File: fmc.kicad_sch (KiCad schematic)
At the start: 2 parts, among them P1 ASP-134604-01, P2 ASP-134604-01

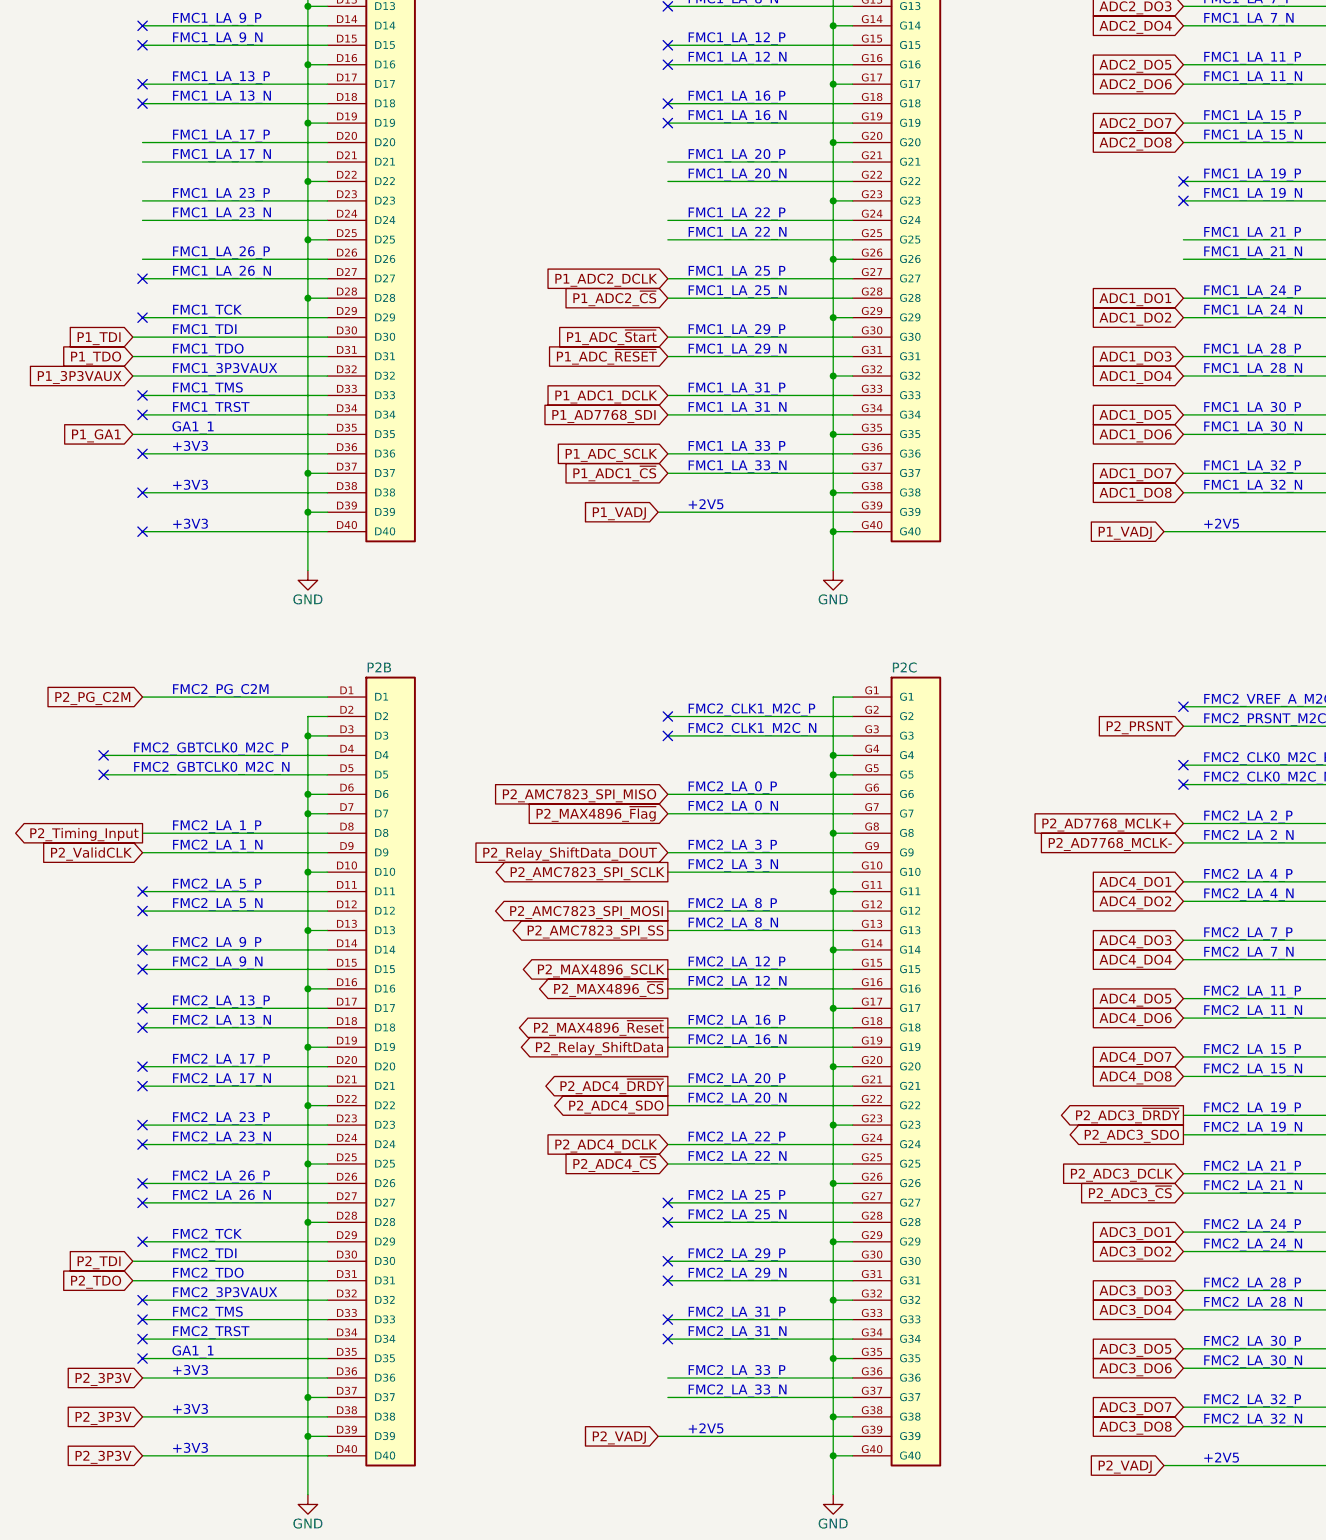
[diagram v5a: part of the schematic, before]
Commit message: Push Version before ADC change from 1.8V to 2.5V I/O
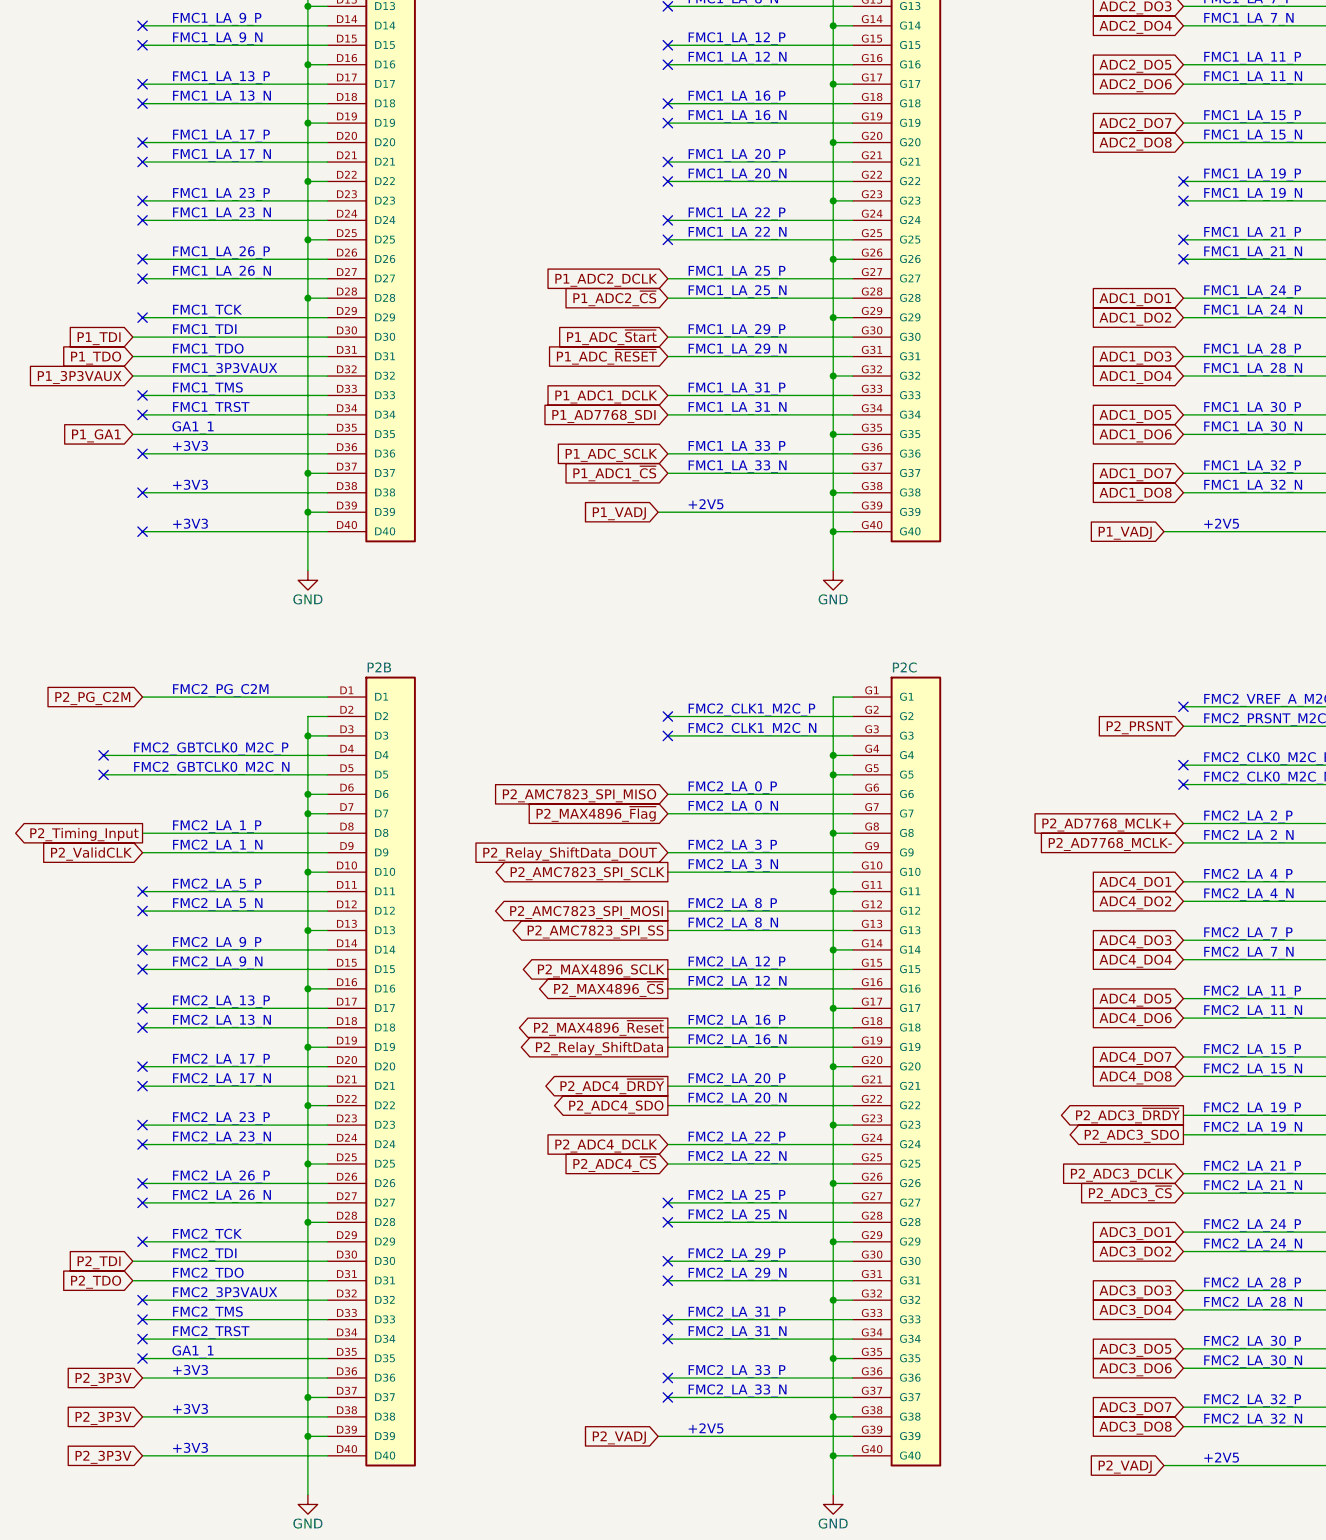
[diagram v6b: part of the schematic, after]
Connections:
- no-connect marks 95 -> 108
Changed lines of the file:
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@@
   )
   (no_connect (at 157.48 49.53))
+  (no_connect (at 293.37 82.55))
   (no_connect (at 157.48 102.87))
   (no_connect (at 87.63 57.15))
@@
   (no_connect (at 87.63 36.83))
   (no_connect (at 157.48 177.8))
+  (no_connect (at 226.06 82.55))
   (no_connect (at 293.37 143.51))
   (no_connect (at 87.63 204.47))
   (no_connect (at 293.37 151.13))
   (no_connect (at 226.06 41.91))
+  (no_connect (at 157.48 80.01))
   (no_connect (at 87.63 146.05))
   (no_connect (at 152.4 31.75))
@@
   (no_connect (at 157.48 185.42))
   (no_connect (at 157.48 213.36))
+  (no_connect (at 226.06 233.68))
   (no_connect (at 87.63 173.99))
   (no_connect (at 157.48 200.66))
   (no_connect (at 87.63 166.37))
+  (no_connect (at 157.48 69.85))
   (no_connect (at 87.63 207.01))
   (no_connect (at 87.63 176.53))
   (no_connect (at 157.48 193.04))
+  (no_connect (at 157.48 77.47))
   (no_connect (at 157.48 39.37))
   (no_connect (at 226.06 24.13))
@@
   (no_connect (at 226.06 218.44))
   (no_connect (at 226.06 44.45))
+  (no_connect (at 226.06 231.14))
+  (no_connect (at 226.06 74.93))
   (no_connect (at 226.06 67.31))
   (no_connect (at 293.37 74.93))
@@
   (no_connect (at 226.06 64.77))
   (no_connect (at 157.48 46.99))
+  (no_connect (at 157.48 72.39))
   (no_connect (at 293.37 21.59))
   (no_connect (at 87.63 163.83))
   (no_connect (at 157.48 115.57))
+  (no_connect (at 157.48 85.09))
   (no_connect (at 157.48 64.77))
   (no_connect (at 293.37 153.67))
@@
   (no_connect (at 152.4 29.21))
   (no_connect (at 157.48 62.23))
+  (no_connect (at 226.06 80.01))
   (no_connect (at 152.4 149.86))
   (no_connect (at 226.06 208.28))
@@
   (no_connect (at 226.06 223.52))
   (no_connect (at 87.63 46.99))
+  (no_connect (at 293.37 85.09))
   (no_connect (at 87.63 26.67))
   (no_connect (at 87.63 77.47))
@@
   (no_connect (at 157.48 198.12))
   (no_connect (at 157.48 223.52))
+  (no_connect (at 226.06 72.39))
   (no_connect (at 157.48 105.41))
   (no_connect (at 226.06 144.78))

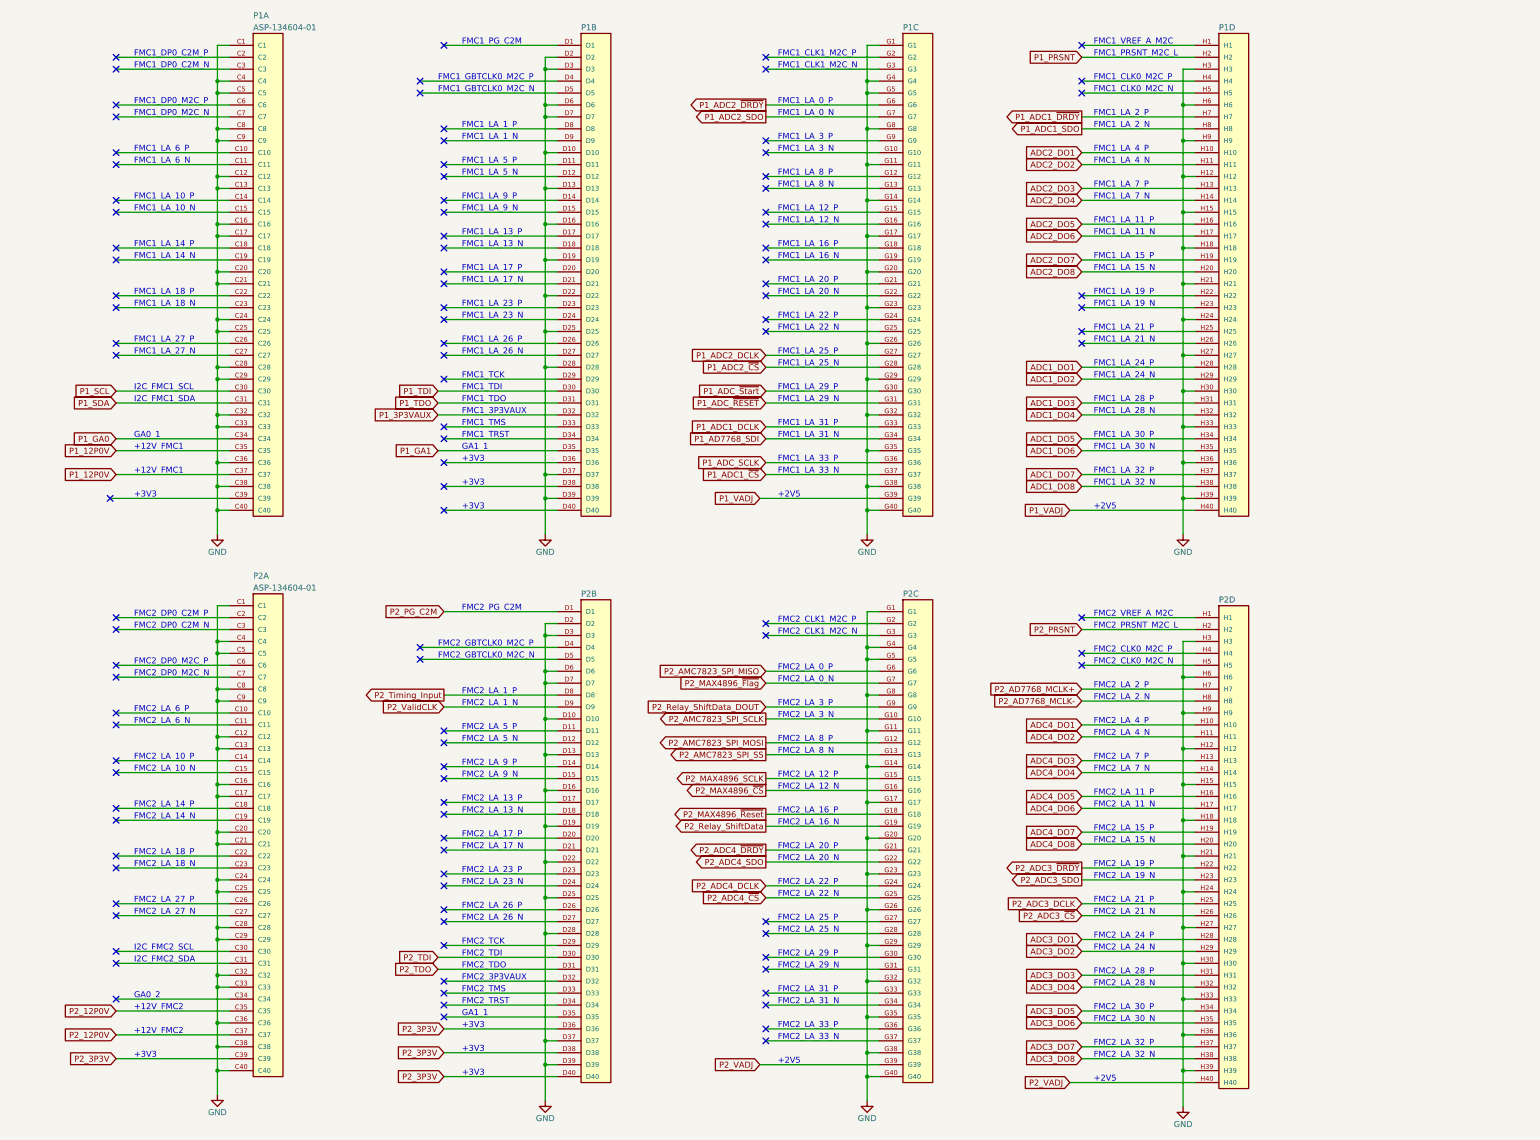
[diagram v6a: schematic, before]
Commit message: Completed Schmatic and Layout
All Schematic and Layout Task are complete with the following exceptions:
- Adjust Silkscreen Layers
- Add Osprey Logo and Serial Number

Note-Removed Files no longer reference in the project
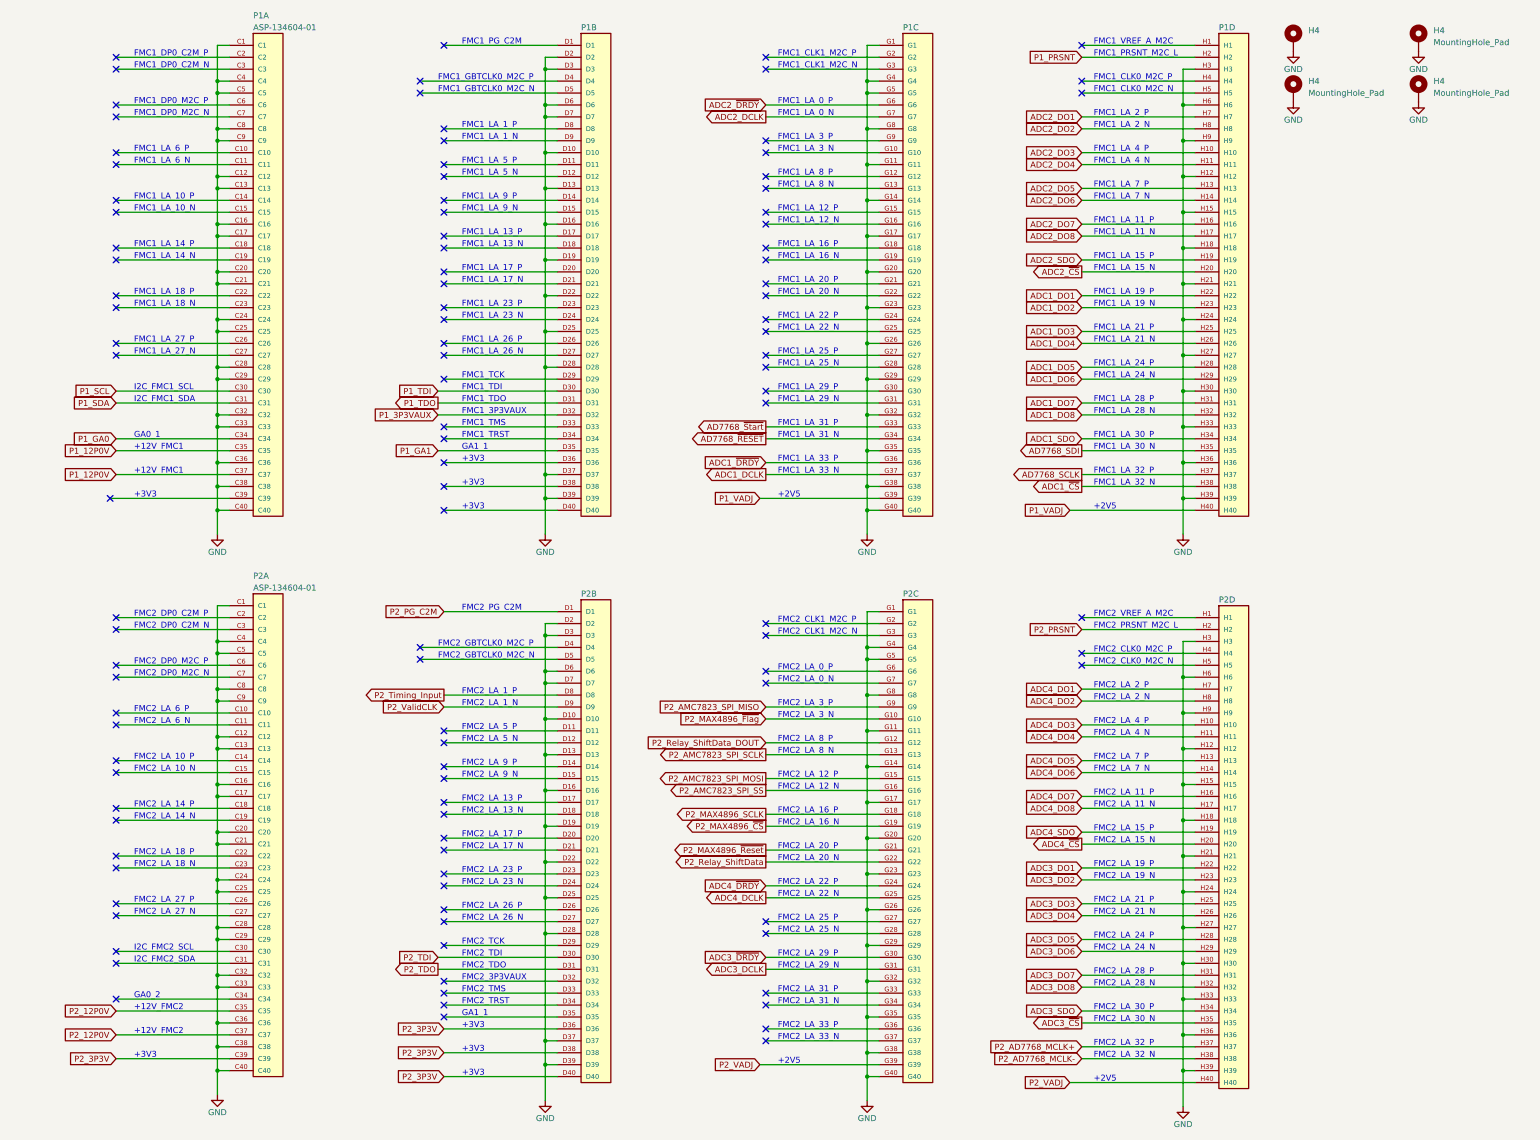
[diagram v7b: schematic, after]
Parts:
- added H4 (x4): MountingHole_Pad, footprints:Mounting Hole 3mm hole 5mm ring, symbol Mechanical:MountingHole_Pad
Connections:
- net P1_ADC1_SDO is gone; now on net ADC2_DO2: P1.H8
- net P1_ADC1_~{DRDY} is gone; now on net ADC2_DO1: P1.H7
- net P2_ADC3_DCLK is gone; now on net ADC3_DO3: P2.H25
- net P2_ADC3_SDO is gone; now on net ADC3_DO2: P2.H23
- net P2_ADC3_~{CS} is gone; now on net ADC3_DO4: P2.H26
- net P2_ADC3_~{DRDY} is gone; now on net ADC3_DO1: P2.H22
- net P2_ADC4_SDO is gone; now on net P2_Relay_ShiftData: P2.G22
- net P2_ADC4_~{DRDY} is gone; now on net P2_MAX4896_~{Reset}: P2.G21
- net ADC1_DO1: now also P1.H22; no longer P1.H28
- net ADC1_DO2: now also P1.H23; no longer P1.H29
- net ADC1_DO3: now also P1.H25; no longer P1.H31
- net ADC1_DO4: now also P1.H26; no longer P1.H32
- net ADC1_DO5: now also P1.H28; no longer P1.H34
- net ADC1_DO6: now also P1.H29; no longer P1.H35
- net ADC1_DO7: now also P1.H31; no longer P1.H37
- net ADC1_DO8: now also P1.H32; no longer P1.H38
- net ADC2_DO1: no longer P1.H10
- net ADC2_DO2: no longer P1.H11
- net ADC2_DO3: now also P1.H10; no longer P1.H13
- net ADC2_DO4: now also P1.H11; no longer P1.H14
- net ADC2_DO5: now also P1.H13; no longer P1.H16
- net ADC2_DO6: now also P1.H14; no longer P1.H17
- net ADC2_DO7: now also P1.H16; no longer P1.H19
- net ADC2_DO8: now also P1.H17; no longer P1.H20
- net ADC3_DO1: no longer P2.H28
- net ADC3_DO2: no longer P2.H29
- net ADC3_DO3: no longer P2.H31
- net ADC3_DO4: no longer P2.H32
- net ADC3_DO5: now also P2.H28; no longer P2.H34
- net ADC3_DO6: now also P2.H29; no longer P2.H35
- net ADC3_DO7: now also P2.H31; no longer P2.H37
- net ADC3_DO8: now also P2.H32; no longer P2.H38
- net ADC4_DO1: now also P2.H7; no longer P2.H10
- net ADC4_DO2: now also P2.H8; no longer P2.H11
- net ADC4_DO3: now also P2.H10; no longer P2.H13
- net ADC4_DO4: now also P2.H11; no longer P2.H14
- net ADC4_DO5: now also P2.H13; no longer P2.H16
- net ADC4_DO6: now also P2.H14; no longer P2.H17
- net ADC4_DO7: now also P2.H16; no longer P2.H19
- net ADC4_DO8: now also P2.H17; no longer P2.H20
- net GND: now also H4.1, H4.1, H4.1, H4.1
- net P2_AD7768_MCLK+: now also P2.H37; no longer P2.H7
- net P2_AD7768_MCLK-: now also P2.H38; no longer P2.H8
- net P2_AMC7823_SPI_MISO: now also P2.G9; no longer P2.G6
- net P2_AMC7823_SPI_MOSI: now also P2.G15; no longer P2.G12
- net P2_AMC7823_SPI_SCLK: now also P2.G13; no longer P2.G10
- net P2_AMC7823_SPI_SS: now also P2.G16; no longer P2.G13
- net P2_MAX4896_SCLK: now also P2.G18; no longer P2.G15
- net P2_MAX4896_~{CS}: now also P2.G19; no longer P2.G16
- net P2_MAX4896_~{Flag}: now also P2.G10; no longer P2.G7
- net P2_MAX4896_~{Reset}: no longer P2.G18
- net P2_Relay_ShiftData: no longer P2.G19
- net P2_Relay_ShiftData_DOUT: now also P2.G12; no longer P2.G9
- net ADC3_~{DRDY}: now reaches P2.G30
- net ADC3_DCLK: now reaches P2.G31
- net P1_AD7768_SDI renamed AD7768_~{RESET}
- net P1_ADC1_DCLK renamed AD7768_~{Start}
- net P1_ADC1_~{CS} renamed ADC1_DCLK
- net P1_ADC2_DCLK: no longer names the net of P1.G27
- net P1_ADC2_SDO renamed ADC2_DCLK
- net P1_ADC2_~{CS}: no longer names the net of P1.G28
- net P1_ADC2_~{DRDY} renamed ADC2_~{DRDY}
- net P1_ADC_SCLK renamed ADC1_~{DRDY}
- net P1_ADC_~{RESET}: no longer names the net of P1.G31
- net P1_ADC_~{Start}: no longer names the net of P1.G30
- net P2_ADC4_DCLK renamed ADC4_~{DRDY}
- net P2_ADC4_~{CS} renamed ADC4_DCLK
- new net AD7768_SCLK: P1.H37
- new net AD7768_SDI: P1.H35
- new net ADC1_SDO: P1.H34
- new net ADC1_~{CS}: P1.H38
- new net ADC2_SDO: P1.H19
- new net ADC2_~{CS}: P1.H20
- new net ADC3_SDO: P2.H34
- new net ADC3_~{CS}: P2.H35
- new net ADC4_SDO: P2.H19
- new net ADC4_~{CS}: P2.H20
